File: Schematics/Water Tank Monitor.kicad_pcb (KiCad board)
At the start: 2 copper layers, 35.3 x 39.4 mm, 19 parts, among them J1 Conn_01x04, J3 Conn_01x04, J4 Conn_01x04, J5 ICSP, J6 FTDI, U1 ATmega328P-A, Y1 16MHz

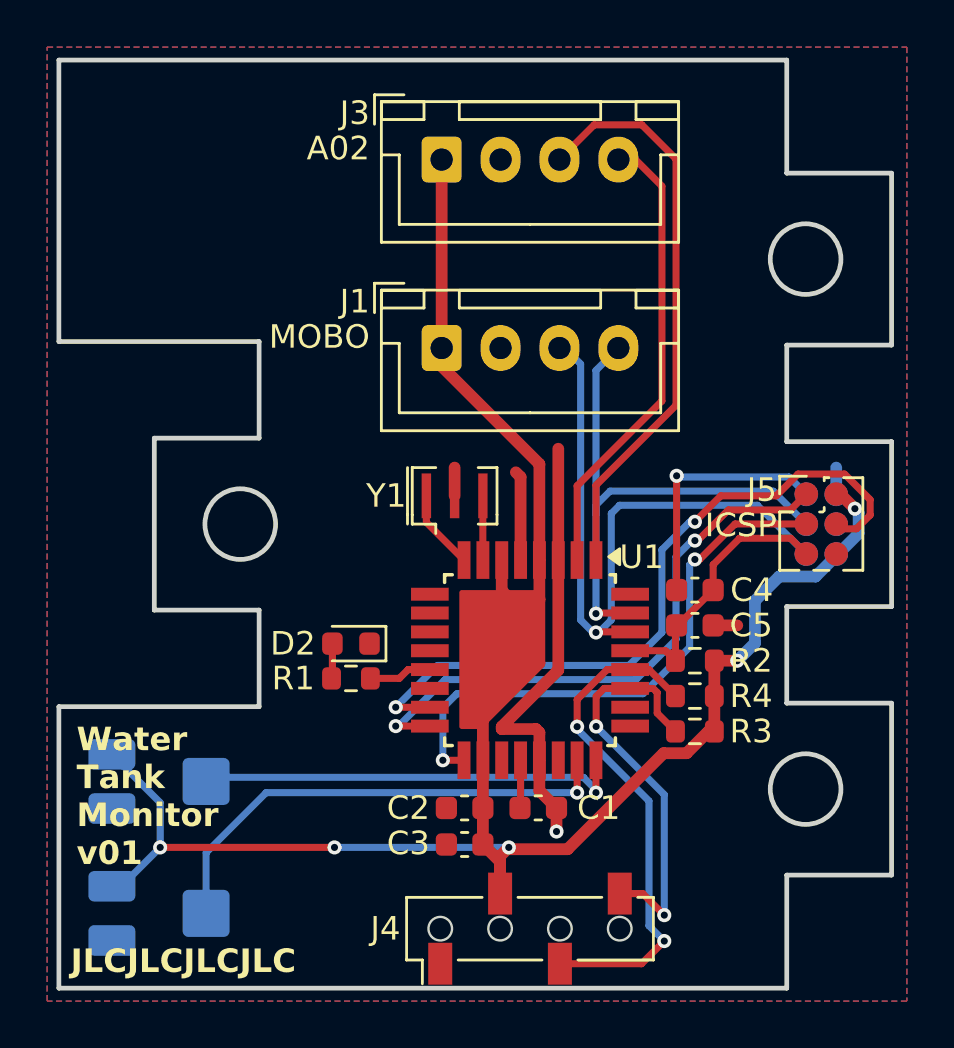
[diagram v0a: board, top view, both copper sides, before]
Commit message: Swap XIAO module to DIP footprint and route v02 board
- Fix U1 footprint/symbol to XIAO-ESP32-C6-DIP (was mismatched SMD)
- Route all nets (RX, TX, SCL, SDA, ACT, VCC) with 45° corners
- Add top/bottom GND pours with stitching vias
- Sync netclass widths across existing copper
- Add C1 decoupling + R3/R4 series resistors at J2 to harden the
  10m Cat5 UART link to the ultrasonic sensor
- Register project footprint library table for XIAO Seeed footprints
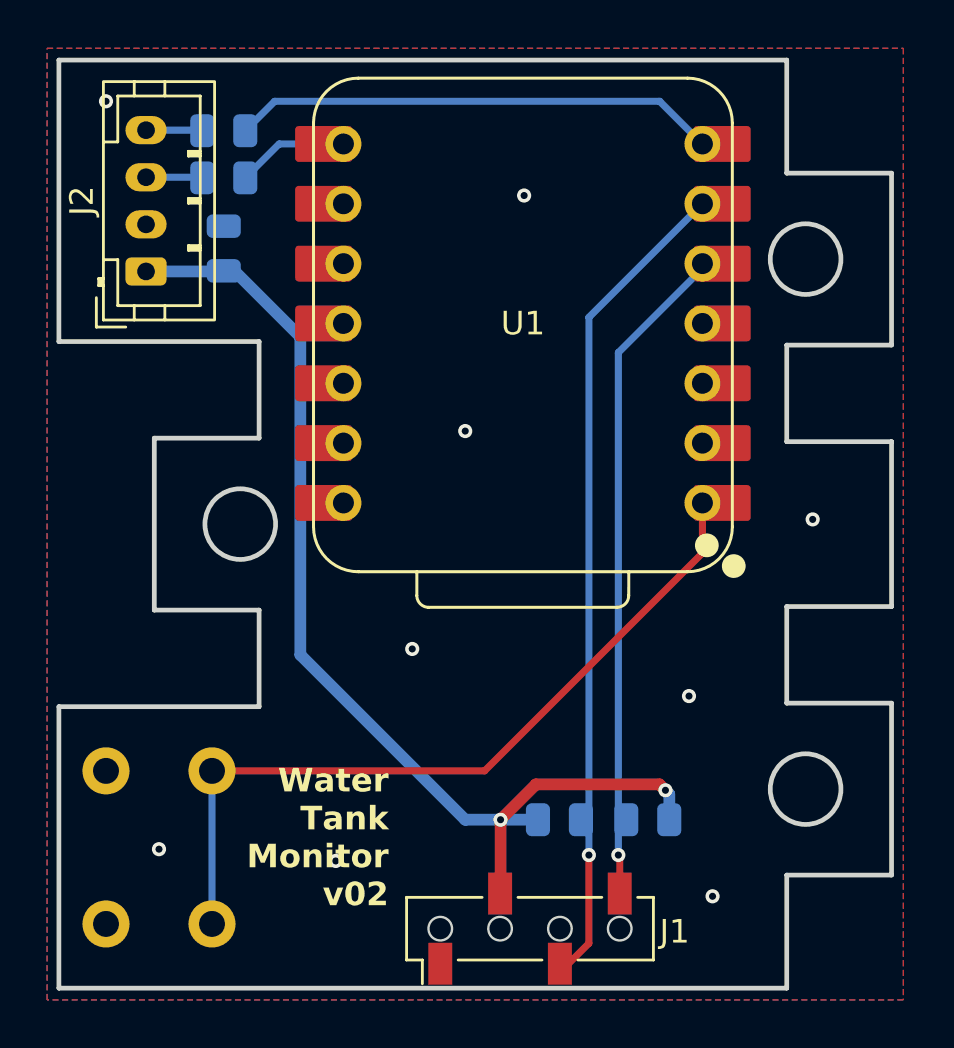
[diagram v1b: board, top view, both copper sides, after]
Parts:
- removed C2, C4, C5: 0.1uF, Capacitor_SMD:C_0603_1608Metric
- removed C3: 10uF, Capacitor_SMD:C_0603_1608Metric
- removed D2: LED, LED_SMD:LED_0603_1608Metric
- removed the J1 at (136.2, 68.7)
- removed J3: Conn_01x04, Connector_JST:JST_XH_B4B-XH-A_1x04_P2.50mm_Vertical
- removed J5: ICSP, Connector_PinHeader_1.27mm:PinHeader_2x03_P1.27mm_Vertical_SMD_pogo
- removed J6: FTDI, Connector_PinHeader_1.27mm:PinHeader_2x03_P1.27mm_Vertical_SMD_pogo
- removed RV1, RV2: 10k, Potentiometer_SMD:Potentiometer_Bourns_3314J_Vertical
- removed Y1: 16MHz, Crystal:Resonator_SMD_Murata_CSTxExxV-3Pin_3.0x1.1mm
- added J2: Conn_01x04, Connector_JST:JST_PH_B4B-PH-K_1x04_P2.00mm_Vertical, F.Cu at (123.7, 65.5)
- added SW1: SW_Push, Button_Switch_THT:SW_PUSH_6mm_H13mm, B.Cu at (126.5, 93.2)
- C1: value 0.1uF -> 100nF; footprint Capacitor_SMD:C_0603_1608Metric -> Capacitor_SMD:C_0805_2012Metric; moved to B.Cu
- R1: value 1k -> 4k7; footprint Resistor_SMD:R_0603_1608Metric -> Resistor_SMD:R_0805_2012Metric; moved to B.Cu
- R2: value 10k -> 4k7; footprint Resistor_SMD:R_0603_1608Metric -> Resistor_SMD_test:R_0805_2012Metric; moved to B.Cu
- R3, R4: value 4.7k -> 100; footprint Resistor_SMD:R_0603_1608Metric -> Resistor_SMD:R_0805_2012Metric; moved to B.Cu
- U1: value ATmega328P-A -> XIAO-ESP32-C6-DIP; footprint Package_QFP:TQFP-32_7x7mm_P0.8mm -> Seeed Studio XIAO Series Library:XIAO-ESP32-C6-DIP
- moved R4 31.2 mm to (127.0, 59.5), turned to 180 degrees
- moved R3 30.9 mm to (127.0, 61.5), turned to 180 degrees
- moved C1 27.2 mm to (127.0, 64.5), turned to 90 degrees
- moved U1 14.3 mm to (139.7, 67.7)
- moved R1 10.7 mm to (141.2, 88.8)
- moved R2 7.04 mm to (145.0, 88.8)
- renumbered J4 to J1
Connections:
- C1 pad 1: Net-(U1-AREF) -> VCC
- J1 pad 2: +3.3V -> VCC
- J1 pad 3: /SCL -> SCL
- J1 pad 4: /SDA -> SDA
- R1 pad 1: Net-(D2-A) -> VCC
- R1 pad 2: Net-(U1-PB1) -> SCL
- R2 pad 1: +3.3V -> VCC
- R2 pad 2: /~{RST} -> SDA
- R3 pad 1: /SDA -> RX
- R3 pad 2: +3.3V -> Net-(J2-Pin_3)
- R4 pad 1: /SCL -> TX
- R4 pad 2: +3.3V -> Net-(J2-Pin_4)
- U1 pad 1: /RXD2 -> ACT
- U1 pad 12: unconnected-(U1-PB0-Pad12) -> VCC
- U1 pad 13: Net-(U1-PB1) -> GND
- U1 pad 2: /TXD2 -> unconnected-(U1-GPIO1_A1_D1-Pad2)_1
- U1 pad 3: GND -> unconnected-(U1-GPIO2_A2_D2-Pad3)_1
- U1 pad 4: +3.3V -> unconnected-(U1-GPIO21_D3-Pad4)
- U1 pad 5: GND -> SDA
- U1 pad 6: +3.3V -> SCL
- U1 pad 7: Net-(U1-XTAL1/PB6) -> TX
- U1 pad 8: Net-(U1-XTAL2/PB7) -> RX
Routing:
- net +3.3V: track 87.7 -> 0.00 mm, vias 5 -> 0
- net VCC: track 0.00 -> 48.1 mm, vias 0 -> 2
- net SCL: track 0.00 -> 35.3 mm, vias 0 -> 1
- net ACT: track 0.00 -> 33.3 mm
- net /MOSI: track 30.6 -> 0.00 mm, vias 2 -> 0
- net /RXD: track 29.1 -> 0.00 mm, vias 1 -> 0
- net SDA: track 0.00 -> 28.7 mm, vias 0 -> 1
- net GND: track 26.3 -> 0.00 mm, vias 1 -> 9
- net /MISO: track 25.0 -> 0.00 mm, vias 2 -> 0
- net /RXD2: track 24.6 -> 0.00 mm
- net /SCK: track 23.8 -> 0.00 mm, vias 2 -> 0
- net /TXD: track 23.3 -> 0.00 mm, vias 1 -> 0
- net /SCL: track 21.8 -> 0.00 mm, vias 2 -> 0
- net /CALIB: track 20.8 -> 0.00 mm, vias 1 -> 0
- net TX: track 0.00 -> 20.7 mm
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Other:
- board text added: "Water Tank Monitor v02"
- board text removed: "A02"
- board text removed: "JLCJLCJLCJLC"
- board text removed: "MOBO"
- board text removed: "Water Tank Monitor v01"
- board text removed: "brightness"
- board text removed: "calibration"
